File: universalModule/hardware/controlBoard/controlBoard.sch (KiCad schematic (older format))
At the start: 0 parts

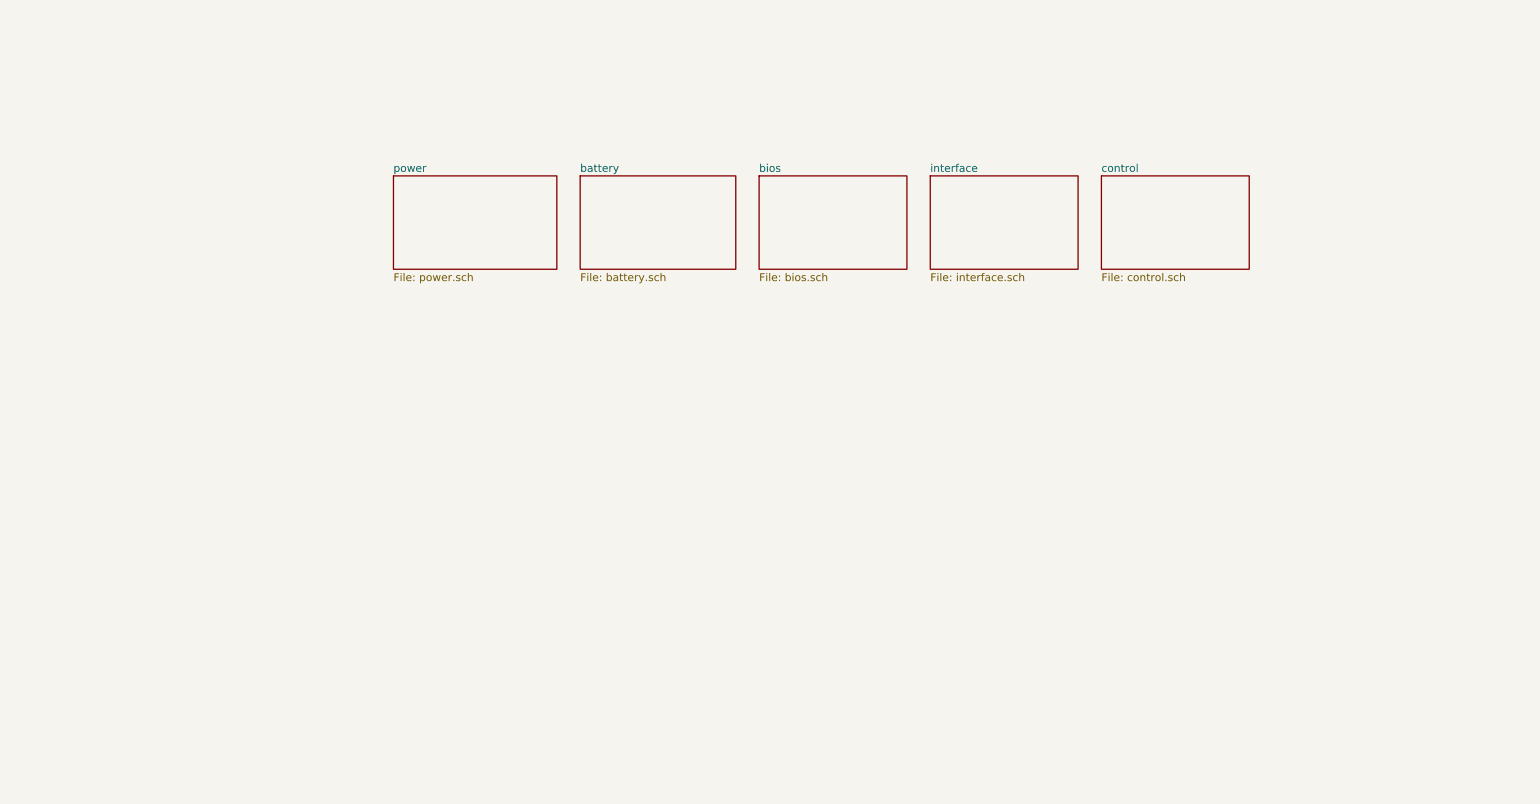
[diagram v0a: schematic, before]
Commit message: universalModule: Route the control boards
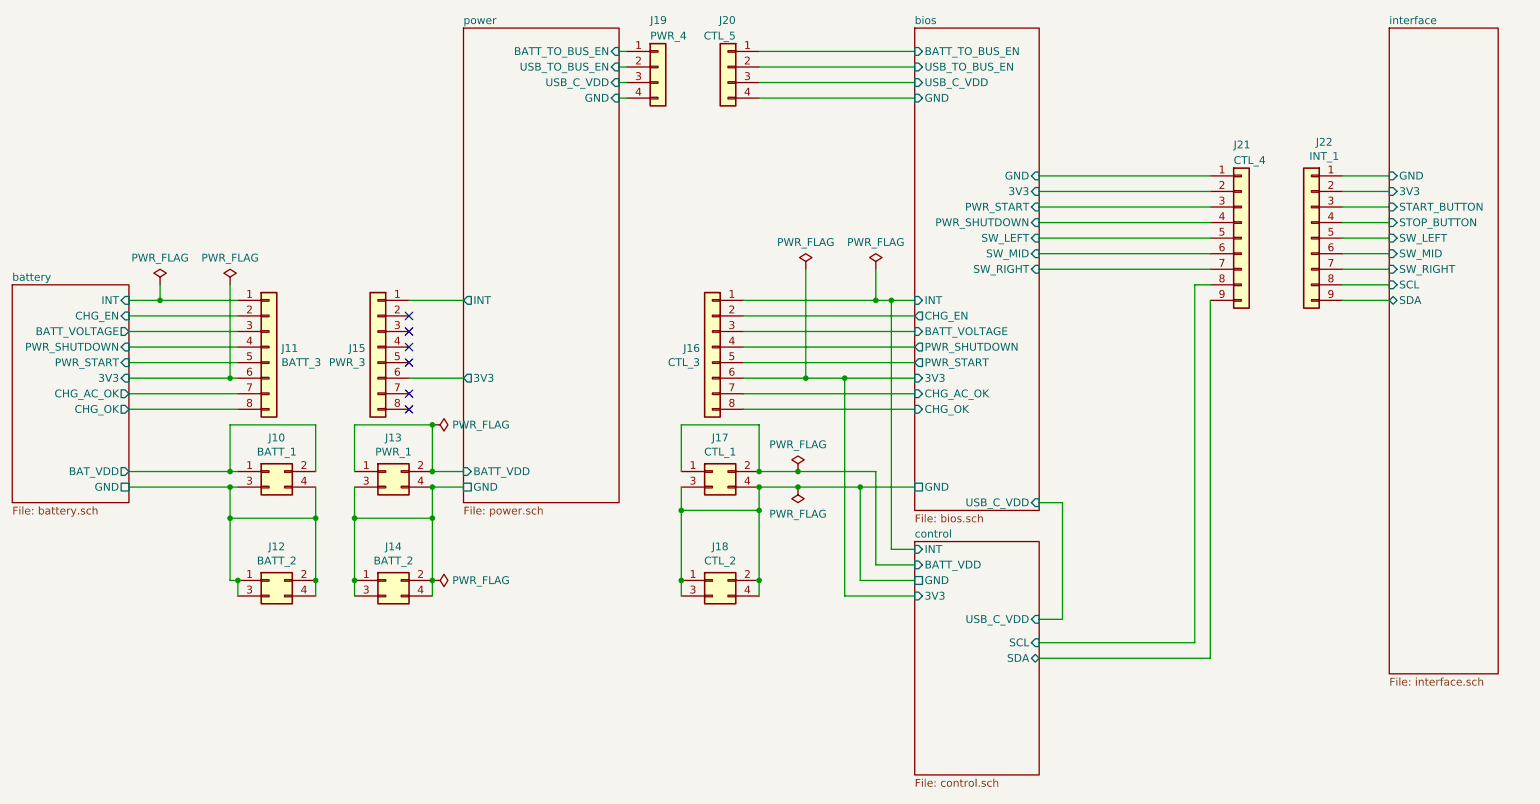
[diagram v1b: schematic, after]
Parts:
- added J10: BATT_1, Connector_PinHeader_2.54mm:PinHeader_2x02_P2.54mm_Vertical, symbol Connector_Generic:Conn_02x02_Odd_Even
- added J11: BATT_3, Connector_PinHeader_2.54mm:PinHeader_1x08_P2.54mm_Vertical, symbol Connector_Generic:Conn_01x08
- added J12, J14: BATT_2, Connector_PinHeader_2.54mm:PinHeader_2x02_P2.54mm_Vertical, symbol Connector_Generic:Conn_02x02_Odd_Even
- added J13: PWR_1, Connector_PinHeader_2.54mm:PinHeader_2x02_P2.54mm_Vertical, symbol Connector_Generic:Conn_02x02_Odd_Even
- added J15: PWR_3, Connector_PinHeader_2.54mm:PinHeader_1x08_P2.54mm_Vertical, symbol Connector_Generic:Conn_01x08
- added J16: CTL_3, Connector_PinHeader_2.54mm:PinHeader_1x08_P2.54mm_Vertical, symbol Connector_Generic:Conn_01x08
- added J17: CTL_1, Connector_PinHeader_2.54mm:PinHeader_2x02_P2.54mm_Vertical, symbol Connector_Generic:Conn_02x02_Odd_Even
- added J18: CTL_2, Connector_PinHeader_2.54mm:PinHeader_2x02_P2.54mm_Vertical, symbol Connector_Generic:Conn_02x02_Odd_Even
- added J19: PWR_4, Connector_PinHeader_2.54mm:PinHeader_1x04_P2.54mm_Vertical, symbol Connector_Generic:Conn_01x04
- added J20: CTL_5, Connector_PinHeader_2.54mm:PinHeader_1x04_P2.54mm_Vertical, symbol Connector_Generic:Conn_01x04
- added J21: CTL_4, Connector_PinHeader_2.00mm:PinHeader_1x09_P2.00mm_Vertical, symbol Connector_Generic:Conn_01x09
- added J22: INT_1, Connector_PinHeader_2.00mm:PinHeader_1x09_P2.00mm_Vertical, symbol Connector_Generic:Conn_01x09
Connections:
- new net battery/3V3: J11.6 (Pin_6)
- new net battery/BATT_VOLTAGE: J11.3 (Pin_3)
- new net battery/BAT_VDD: J10.1 (Pin_1), J10.2 (Pin_2)
- new net battery/CHG_AC_OK: J11.7 (Pin_7)
- new net battery/CHG_EN: J11.2 (Pin_2)
- new net battery/CHG_OK: J11.8 (Pin_8)
- new net battery/GND: J10.3 (Pin_3), J10.4 (Pin_4), J12.1 (Pin_1), J12.2 (Pin_2), J12.3 (Pin_3), J12.4 (Pin_4)
- new net battery/INT: J11.1 (Pin_1)
- new net battery/PWR_SHUTDOWN: J11.4 (Pin_4)
- new net battery/PWR_START: J11.5 (Pin_5)
- new net bios/3V3: J16.6 (Pin_6)
- new net bios/3V3: J21.2 (Pin_2)
- new net bios/BATT_TO_BUS_EN: J20.1 (Pin_1)
- new net bios/BATT_VOLTAGE: J16.3 (Pin_3)
- new net bios/CHG_AC_OK: J16.7 (Pin_7)
- new net bios/CHG_EN: J16.2 (Pin_2)
- new net bios/CHG_OK: J16.8 (Pin_8)
- new net bios/GND: J17.3 (Pin_3), J17.4 (Pin_4), J18.1 (Pin_1), J18.2 (Pin_2), J18.3 (Pin_3), J18.4 (Pin_4)
- new net bios/GND: J21.1 (Pin_1)
- new net bios/GND: J20.4 (Pin_4)
- new net bios/INT: J16.1 (Pin_1)
- new net bios/PWR_SHUTDOWN: J16.4 (Pin_4)
- new net bios/PWR_SHUTDOWN: J21.4 (Pin_4)
- new net bios/PWR_START: J16.5 (Pin_5)
- new net bios/PWR_START: J21.3 (Pin_3)
- new net bios/SW_LEFT: J21.5 (Pin_5)
- new net bios/SW_MID: J21.6 (Pin_6)
- new net bios/SW_RIGHT: J21.7 (Pin_7)
- new net bios/USB_C_VDD: J20.3 (Pin_3)
- new net bios/USB_TO_BUS_EN: J20.2 (Pin_2)
- new net control/BATT_VDD: J17.1 (Pin_1), J17.2 (Pin_2)
- new net control/SCL: J21.8 (Pin_8)
- new net control/SDA: J21.9 (Pin_9)
- new net interface/3V3: J22.2 (Pin_2)
- new net interface/GND: J22.1 (Pin_1)
- new net interface/SCL: J22.8 (Pin_8)
- new net interface/SDA: J22.9 (Pin_9)
- new net interface/START_BUTTON: J22.3 (Pin_3)
- new net interface/STOP_BUTTON: J22.4 (Pin_4)
- new net interface/SW_LEFT: J22.5 (Pin_5)
- new net interface/SW_MID: J22.6 (Pin_6)
- new net interface/SW_RIGHT: J22.7 (Pin_7)
- new net power/3V3: J15.6 (Pin_6)
- new net power/BATT_TO_BUS_EN: J19.1 (Pin_1)
- new net power/BATT_VDD: J13.1 (Pin_1), J13.2 (Pin_2)
- new net power/GND: J13.3 (Pin_3), J13.4 (Pin_4), J14.1 (Pin_1), J14.2 (Pin_2), J14.3 (Pin_3), J14.4 (Pin_4)
- new net power/GND: J19.4 (Pin_4)
- new net power/INT: J15.1 (Pin_1)
- new net power/USB_C_VDD: J19.3 (Pin_3)
- new net power/USB_TO_BUS_EN: J19.2 (Pin_2)
- no-connect marks 0 -> 6

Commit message: universalModule: Fine tune the control board
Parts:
- added H1, H2, H3, H4, H5, H6: MountingHole, MountingHole:MountingHole_2.1mm, symbol Mechanical:MountingHole
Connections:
- net bios/3V3 is gone; now on net bios/3V3: J21.2 (Pin_2)
- net bios/GND is gone; now on net bios/GND: J20.4 (Pin_4)
- net bios/PWR_SHUTDOWN is gone; now on net bios/PWR_SHUTDOWN: J21.4 (Pin_4)
- net bios/PWR_START is gone; now on net bios/PWR_START: J21.3 (Pin_3)
- net bios/USB_C_VDD is gone; now on net bios/USB_C_VDD: J20.3 (Pin_3)
- net power/GND is gone; now on net power/GND: J19.4 (Pin_4)
- net bios/3V3: no longer J16.6 (Pin_6)
- net bios/GND: no longer J17.3 (Pin_3), J17.4 (Pin_4), J18.1 (Pin_1), J18.2 (Pin_2), J18.3 (Pin_3), J18.4 (Pin_4)
- net bios/PWR_SHUTDOWN: no longer J16.4 (Pin_4)
- net bios/PWR_START: no longer J16.5 (Pin_5)
- net power/GND: no longer J13.3 (Pin_3), J13.4 (Pin_4), J14.1 (Pin_1), J14.2 (Pin_2), J14.3 (Pin_3), J14.4 (Pin_4)
- new net bios/3V3: J16.6 (Pin_6)
- new net bios/GND: J17.3 (Pin_3), J17.4 (Pin_4), J18.1 (Pin_1), J18.2 (Pin_2), J18.3 (Pin_3), J18.4 (Pin_4)
- new net bios/PWR_SHUTDOWN: J16.4 (Pin_4)
- new net bios/PWR_START: J16.5 (Pin_5)
- new net power/GND: J13.3 (Pin_3), J13.4 (Pin_4), J14.1 (Pin_1), J14.2 (Pin_2), J14.3 (Pin_3), J14.4 (Pin_4)
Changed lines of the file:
@@
 Wire Wire Line
 	6000 3200 6450 3200
+$Comp
+L Mechanical:MountingHole H4
+U 1 1 5DE07B9A
+P 750 2200
+F 0 "H4" H 850 2246 50  0000 L CNN
+F 1 "MountingHole" H 850 2155 50  0000 L CNN
+F 2 "MountingHole:MountingHole_2.1mm" H 750 2200 50  0001 C CNN
+F 3 "~" H 750 2200 50  0001 C CNN
+	1    750  2200
+	1    0    0    -1
+$EndComp
+$Comp
+L Mechanical:MountingHole H3
+U 1 1 5DE0904B
+P 750 2000
+F 0 "H3" H 850 2046 50  0000 L CNN
+F 1 "MountingHole" H 850 1955 50  0000 L CNN
+F 2 "MountingHole:MountingHole_2.1mm" H 750 2000 50  0001 C CNN
+F 3 "~" H 750 2000 50  0001 C CNN
+	1    750  2000
+	1    0    0    -1
+$EndComp
+$Comp
+L Mechanical:MountingHole H2
+U 1 1 5DE091EE
+P 750 1800
+F 0 "H2" H 850 1846 50  0000 L CNN
+F 1 "MountingHole" H 850 1755 50  0000 L CNN
+F 2 "MountingHole:MountingHole_2.1mm" H 750 1800 50  0001 C CNN
+F 3 "~" H 750 1800 50  0001 C CNN
+	1    750  1800
+	1    0    0    -1
+$EndComp
+$Comp
+L Mechanical:MountingHole H1
+U 1 1 5DE0947E
+P 750 1600
+F 0 "H1" H 850 1646 50  0000 L CNN
+F 1 "MountingHole" H 850 1555 50  0000 L CNN
+F 2 "MountingHole:MountingHole_2.1mm" H 750 1600 50  0001 C CNN
+F 3 "~" H 750 1600 50  0001 C CNN
+	1    750  1600
+	1    0    0    -1
+$EndComp
+$Comp
+L Mechanical:MountingHole H5
+U 1 1 5DE0BB0E
+P 9600 5300
+F 0 "H5" H 9700 5346 50  0000 L CNN
+F 1 "MountingHole" H 9700 5255 50  0000 L CNN
+F 2 "MountingHole:MountingHole_2.1mm" H 9600 5300 50  0001 C CNN
+F 3 "~" H 9600 5300 50  0001 C CNN
+	1    9600 5300
+	1    0    0    -1
+$EndComp
+$Comp
+L Mechanical:MountingHole H6
+U 1 1 5DE0DC9E
+P 9600 5500
+F 0 "H6" H 9700 5546 50  0000 L CNN
+F 1 "MountingHole" H 9700 5455 50  0000 L CNN
+F 2 "MountingHole:MountingHole_2.1mm" H 9600 5500 50  0001 C CNN
+F 3 "~" H 9600 5500 50  0001 C CNN
+	1    9600 5500
+	1    0    0    -1
+$EndComp
 $EndSCHEMATC
